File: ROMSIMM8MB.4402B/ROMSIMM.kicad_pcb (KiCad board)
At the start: 4 copper layers, 97.8 x 25 mm, 39 parts, among them J1 ROM, SW1 ROM Select, U1 MX29LV640, U10 74AHC245, U11 LD1117S33, U12 74LVC1G02GW, U2 MX29LV640, U3 74AHC245, U4 74AHC245, U5 74AHC245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

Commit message: Finished rev. B board
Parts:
- added R3: 100, stdpads:R_0603, F.Cu at (118.8, 119.7)
- H1, H2, H3, H4: footprint stdpads:PasteHole_1.1mm_PTH -> stdpads:PasteHole_1.152mm_NPTH
- R1: footprint stdpads:R_0805 -> stdpads:R_0603
- R2: value 100 -> 3k3; footprint stdpads:R_0805 -> stdpads:R_0603
- SW1: value ROM Select -> ROM Sel.; footprint Button_Switch_SMD:SW_DIP_SPSTx01_Slide_6.7x4.1mm_W8.61mm_P2.54mm_LowProfile -> stdpads:SW_DIP_SPSTx02_Slide_DSHP02TS_P1.27mm
- U11: value LD1117S33 -> XC6206P332MR; footprint stdpads:SOT-223 -> stdpads:SOT-23
- moved R2 39.2 mm to (155.4, 105.8)
- moved U11 2.94 mm to (78.3, 111.2)
- moved SW1 2.05 mm to (159.5, 110.9), turned to 0 degrees
- moved R1 2.03 mm to (155.4, 104.3), turned to 180 degrees
- turned U1 to 270 degrees
- turned U10 to 180 degrees
- turned U2 to 270 degrees
- turned U3 to 180 degrees
- turned U4 to 180 degrees
- turned U5 to 180 degrees
- turned U6 to 180 degrees
- turned U7 to 180 degrees
- turned U8 to 180 degrees
- turned U9 to 180 degrees
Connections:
- R1 pad 1: +3V3 -> /RA23
- R1 pad 2: /RA23 -> +3V3
- R2 pad 1: /DdirR -> /RA22sw
- R2 pad 2: /Ddir -> +3V3
- SW1 pad 1: /RA23 -> /RA22
- U1 pad 10: /RA22 -> /RA22sw
- U2 pad 10: /RA22 -> /RA22sw
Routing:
- net /RA22sw: track 0.00 -> 79.0 mm, vias 0 -> 3
- net /RA22: track 60.4 -> 28.1 mm, vias 3 -> 2
- net +3V3: track 68.6 -> 59.2 mm, vias 79 -> 75
- net +5V: track 156.4 -> 164.2 mm, vias 5 -> 8
- net GND: track 102.8 -> 97.6 mm, vias 169 -> 159
- net /RA23: track 94.6 -> 95.5 mm
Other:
- board text added: "4402B"
- board text added: ": none : Sys6 : Sys7"
- board text added: "ROM Disk"
- board text removed: "4402A"

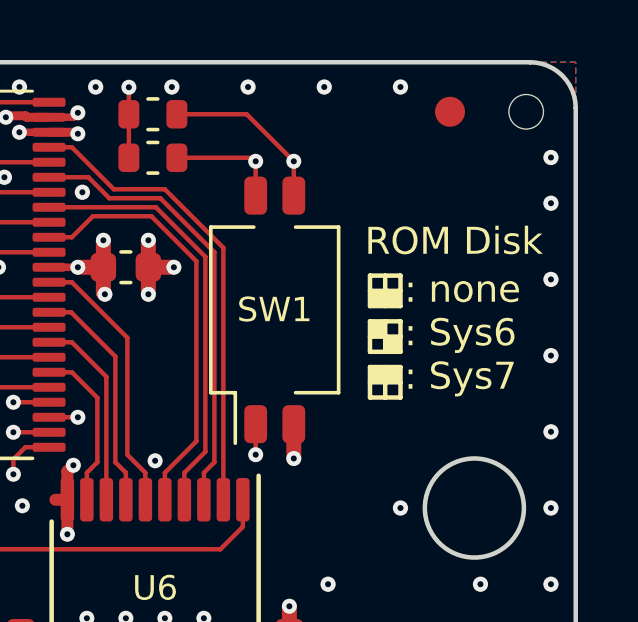
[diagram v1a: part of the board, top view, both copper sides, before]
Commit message: Make silkscreen setting text clearer
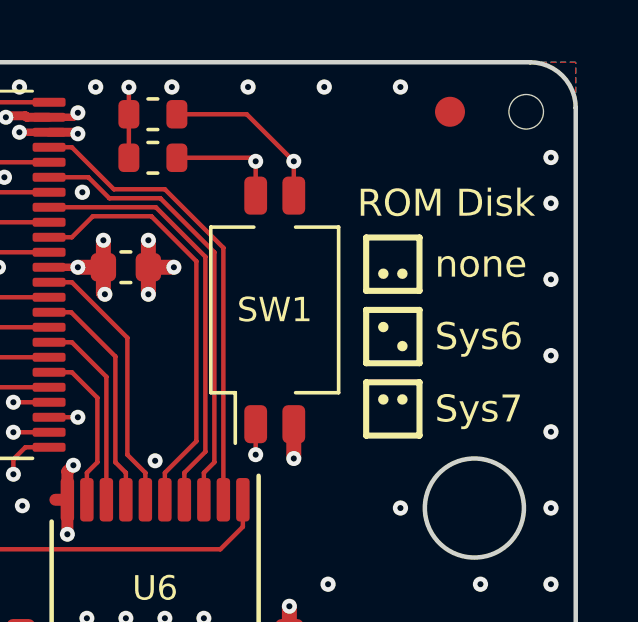
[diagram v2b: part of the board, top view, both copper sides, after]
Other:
- board text added: "Sys6"
- board text added: "Sys7"
- board text added: "none"
- board text removed: ": none : Sys6 : Sys7"

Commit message: Fabbed
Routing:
- net /RA22: track 28.1 -> 30.9 mm
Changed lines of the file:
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@@
     (thickness 1.6)
     (drawings 43)
-    (tracks 1427)
+    (tracks 1430)
     (zones 0)
     (modules 40)
@@
     )
     (fp_text value "ROM Sel." (at 0 1.905 180) (layer F.Fab)
-      (effects (font (size 0.508 0.508) (thickness 0.127)))
+      (effects (font (size 0.8128 0.8128) (thickness 0.2032)))
     )
     (fp_text user on (at -1.5525 0.055 90) (layer F.Fab)
@@
       (effects (font (size 0.8128 0.8128) (thickness 0.2032)))
     )
-    (fp_line (start -2.39 -4.7) (end -2.39 4.7) (layer F.CrtYd) (width 0.05))
-    (fp_line (start 2.39 -4.7) (end -2.39 -4.7) (layer F.CrtYd) (width 0.05))
-    (fp_line (start 2.39 4.7) (end 2.39 -4.7) (layer F.CrtYd) (width 0.05))
-    (fp_line (start -2.39 4.7) (end 2.39 4.7) (layer F.CrtYd) (width 0.05))
+    (fp_line (start -2.413 -4.826) (end -2.413 4.826) (layer F.CrtYd) (width 0.05))
+    (fp_line (start 2.413 -4.826) (end -2.413 -4.826) (layer F.CrtYd) (width 0.05))
+    (fp_line (start 2.413 4.826) (end 2.413 -4.826) (layer F.CrtYd) (width 0.05))
+    (fp_line (start -2.413 4.826) (end 2.413 4.826) (layer F.CrtYd) (width 0.05))
     (fp_line (start 0.695 -2.76) (end 2.13 -2.76) (layer F.SilkS) (width 0.12))
     (fp_line (start 0.695 2.76) (end 2.13 2.76) (layer F.SilkS) (width 0.12))
@@
     (fp_line (start -2.07 -2.7) (end 2.07 -2.7) (layer F.Fab) (width 0.1))
     (fp_line (start -2.07 1.7) (end -2.07 -2.7) (layer F.Fab) (width 0.1))
-    (pad 4 smd roundrect (at -0.635 -3.81 90) (size 1.27 0.76) (layers F.Cu F.Paste F.Mask) (roundrect_rratio 0.25)
+    (pad 4 smd roundrect (at -0.635 -3.81 90) (size 1.524 0.76) (layers F.Cu F.Paste F.Mask) (roundrect_rratio 0.25)
       (net 132 /RA22sw))
-    (pad 3 smd roundrect (at 0.635 -3.81 90) (size 1.27 0.76) (layers F.Cu F.Paste F.Mask) (roundrect_rratio 0.25)
+    (pad 3 smd roundrect (at 0.635 -3.81 90) (size 1.524 0.76) (layers F.Cu F.Paste F.Mask) (roundrect_rratio 0.25)
       (net 129 /RA23))
-    (pad 2 smd roundrect (at 0.635 3.81 90) (size 1.27 0.76) (layers F.Cu F.Paste F.Mask) (roundrect_rratio 0.25)
+    (pad 2 smd roundrect (at 0.635 3.81 90) (size 1.524 0.76) (layers F.Cu F.Paste F.Mask) (roundrect_rratio 0.25)
       (net 7 GND))
-    (pad 1 smd roundrect (at -0.635 3.81 90) (size 1.27 0.76) (layers F.Cu F.Paste F.Mask) (roundrect_rratio 0.25)
+    (pad 1 smd roundrect (at -0.635 3.81 90) (size 1.524 0.76) (layers F.Cu F.Paste F.Mask) (roundrect_rratio 0.25)
       (net 121 /RA22))
     (model ${KISYS3DMOD}/Button_Switch_SMD.3dshapes/SW_DIP_SPSTx02_Slide_KingTek_DSHP02TS_W7.62mm_P1.27mm.wrl
@@
   (segment (start 131.8 119.45) (end 130.45 118.1) (width 0.15) (layer F.Cu) (net 120))
   (segment (start 136.85 117.2) (end 136.85 118.1) (width 0.15) (layer F.Cu) (net 120))
-  (via (at 158.877 115.697) (size 0.5) (drill 0.2) (layers F.Cu B.Cu) (net 121))
-  (segment (start 158.877 114.681) (end 158.877 115.697) (width 0.15) (layer F.Cu) (net 121))
   (via (at 137.5 113.75) (size 0.5) (drill 0.2) (layers F.Cu B.Cu) (net 121))
   (segment (start 137.5 113.75) (end 137.5 117.2) (width 0.15) (layer F.Cu) (net 121))
   (segment (start 139.25 112) (end 137.5 113.75) (width 0.15) (layer In2.Cu) (net 121))
+  (segment (start 159.6 116.42) (end 155.18 112) (width 0.15) (layer In2.Cu) (net 121))
   (segment (start 155.18 112) (end 139.25 112) (width 0.15) (layer In2.Cu) (net 121))
-  (segment (start 158.877 115.697) (end 155.18 112) (width 0.15) (layer In2.Cu) (net 121))
+  (segment (start 159.6 116.8) (end 159.6 116.42) (width 0.15) (layer In2.Cu) (net 121))
+  (via (at 159.6 116.8) (size 0.5) (drill 0.2) (layers F.Cu B.Cu) (net 121))
+  (segment (start 159.6 116.45) (end 158.877 115.727) (width 0.15) (layer F.Cu) (net 121))
+  (segment (start 158.877 115.727) (end 158.877 114.681) (width 0.15) (layer F.Cu) (net 121))
+  (segment (start 159.6 116.8) (end 159.6 116.45) (width 0.15) (layer F.Cu) (net 121))
   (via (at 133.45 109.95) (size 0.5) (drill 0.2) (layers F.Cu B.Cu) (net 129))
   (segment (start 132.49 109.95) (end 133.45 109.95) (width 0.15) (layer F.Cu) (net 129))
@@
   (segment (start 87.9 114.8) (end 88.55 115.45) (width 0.15) (layer In2.Cu) (net 129))
   (segment (start 87.9 111.2) (end 87.9 114.8) (width 0.15) (layer In2.Cu) (net 129))
-  (segment (start 158.579 104.35) (end 156.25 104.35) (width 0.15) (layer F.Cu) (net 129))
-  (segment (start 160.147 105.918) (end 158.579 104.35) (width 0.15) (layer F.Cu) (net 129))
+  (segment (start 160.147 107.061) (end 160.147 105.791) (width 0.15) (layer F.Cu) (net 129))
   (segment (start 133.95 110.45) (end 133.45 109.95) (width 0.15) (layer In2.Cu) (net 129))
   (segment (start 148.25 110.45) (end 133.95 110.45) (width 0.15) (layer In2.Cu) (net 129))
-  (segment (start 149 111.2) (end 148.25 110.45) (width 0.15) (layer In2.Cu) (net 129))
-  (segment (start 160.147 105.918) (end 160.147 106.299) (width 0.15) (layer In2.Cu) (net 129))
-  (segment (start 160.147 106.299) (end 155.246 111.2) (width 0.15) (layer In2.Cu) (net 129))
-  (via (at 160.147 105.918) (size 0.5) (drill 0.2) (layers F.Cu B.Cu) (net 129))
-  (segment (start 160.147 107.061) (end 160.147 105.918) (width 0.15) (layer F.Cu) (net 129))
+  (segment (start 160.147 105.791) (end 158.706 104.35) (width 0.15) (layer F.Cu) (net 129))
+  (segment (start 160.147 105.791) (end 160.147 106.299) (width 0.15) (layer In2.Cu) (net 129))
   (segment (start 155.246 111.2) (end 149 111.2) (width 0.15) (layer In2.Cu) (net 129))
+  (segment (start 158.706 104.35) (end 156.25 104.35) (width 0.15) (layer F.Cu) (net 129))
+  (segment (start 160.147 106.299) (end 155.246 111.2) (width 0.15) (layer In2.Cu) (net 129))
+  (segment (start 149 111.2) (end 148.25 110.45) (width 0.15) (layer In2.Cu) (net 129))
+  (via (at 160.147 105.791) (size 0.5) (drill 0.2) (layers F.Cu B.Cu) (net 129))
   (via (at 105.1 118.35) (size 0.5) (drill 0.2) (layers F.Cu B.Cu) (net 130))
   (segment (start 105.1 117.2) (end 105.1 118.35) (width 0.15) (layer F.Cu) (net 130))
@@
   (segment (start 131.4 108.45) (end 129 110.85) (width 0.15) (layer In2.Cu) (net 132))
   (segment (start 131.55 108.45) (end 131.4 108.45) (width 0.15) (layer In2.Cu) (net 132))
-  (segment (start 158.759 105.8) (end 156.25 105.8) (width 0.15) (layer F.Cu) (net 132))
-  (segment (start 158.877 105.918) (end 158.877 107.061) (width 0.15) (layer F.Cu) (net 132))
-  (segment (start 158.877 105.918) (end 158.759 105.8) (width 0.15) (layer F.Cu) (net 132))
-  (via (at 158.877 105.918) (size 0.5) (drill 0.2) (layers F.Cu B.Cu) (net 132))
   (segment (start 135.8 108.45) (end 131.55 108.45) (width 0.15) (layer In2.Cu) (net 132))
-  (segment (start 158.877 105.918) (end 158.659 105.7) (width 0.15) (layer In2.Cu) (net 132))
-  (segment (start 148.8 106.95) (end 137.3 106.95) (width 0.15) (layer In2.Cu) (net 132))
   (segment (start 137.3 106.95) (end 135.8 108.45) (width 0.15) (layer In2.Cu) (net 132))
-  (segment (start 158.659 105.7) (end 150.05 105.7) (width 0.15) (layer In2.Cu) (net 132))
+  (segment (start 148.8 106.95) (end 137.3 106.95) (width 0.15) (layer In2.Cu) (net 132))
   (segment (start 150.05 105.7) (end 148.8 106.95) (width 0.15) (layer In2.Cu) (net 132))
+  (segment (start 158.786 105.7) (end 150.05 105.7) (width 0.15) (layer In2.Cu) (net 132))
+  (segment (start 158.877 105.791) (end 158.786 105.7) (width 0.15) (layer In2.Cu) (net 132))
+  (segment (start 158.868 105.8) (end 156.25 105.8) (width 0.15) (layer F.Cu) (net 132))
+  (via (at 158.877 105.791) (size 0.5) (drill 0.2) (layers F.Cu B.Cu) (net 132))
+  (segment (start 158.877 105.791) (end 158.877 107.061) (width 0.15) (layer F.Cu) (net 132))
+  (segment (start 158.877 105.791) (end 158.868 105.8) (width 0.15) (layer F.Cu) (net 132))
   (zone (net 7) (net_name GND) (layer F.Cu) (hatch edge 0.508)
     (connect_pads (clearance 0.154))
